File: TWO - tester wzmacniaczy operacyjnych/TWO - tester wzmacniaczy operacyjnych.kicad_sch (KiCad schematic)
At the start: 21 parts

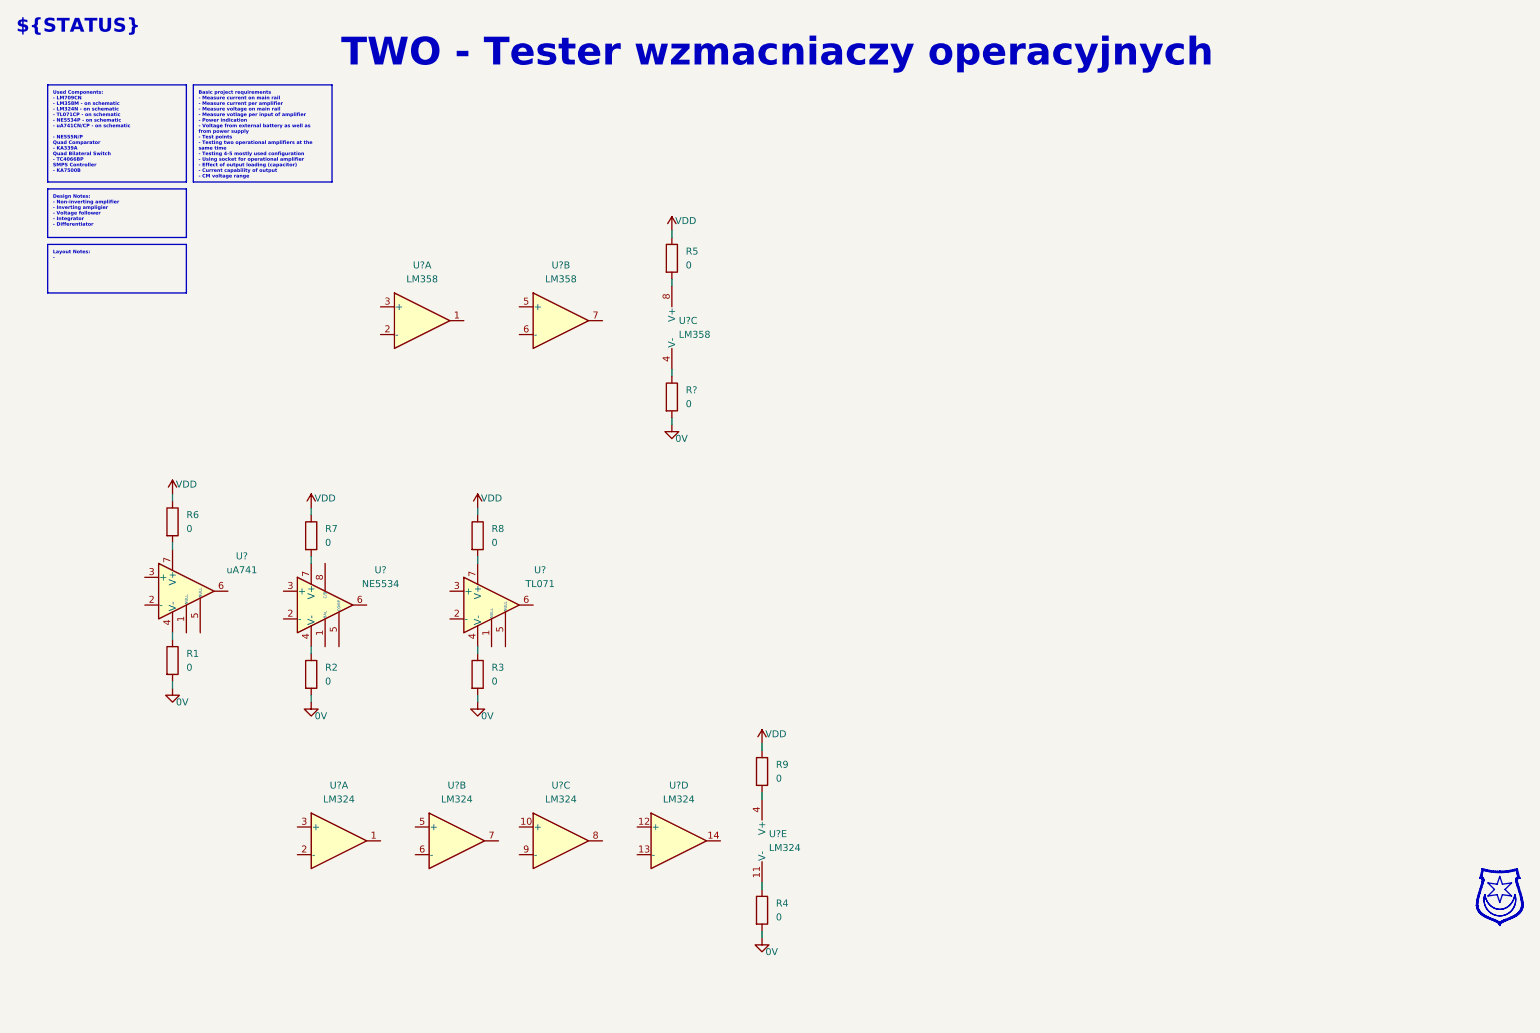
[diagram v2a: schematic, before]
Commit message: Added 50R input, variant with SMD components, input capacitor for AC signal, output capacitance, outputresistor agains short circuit, decoupling capacitors
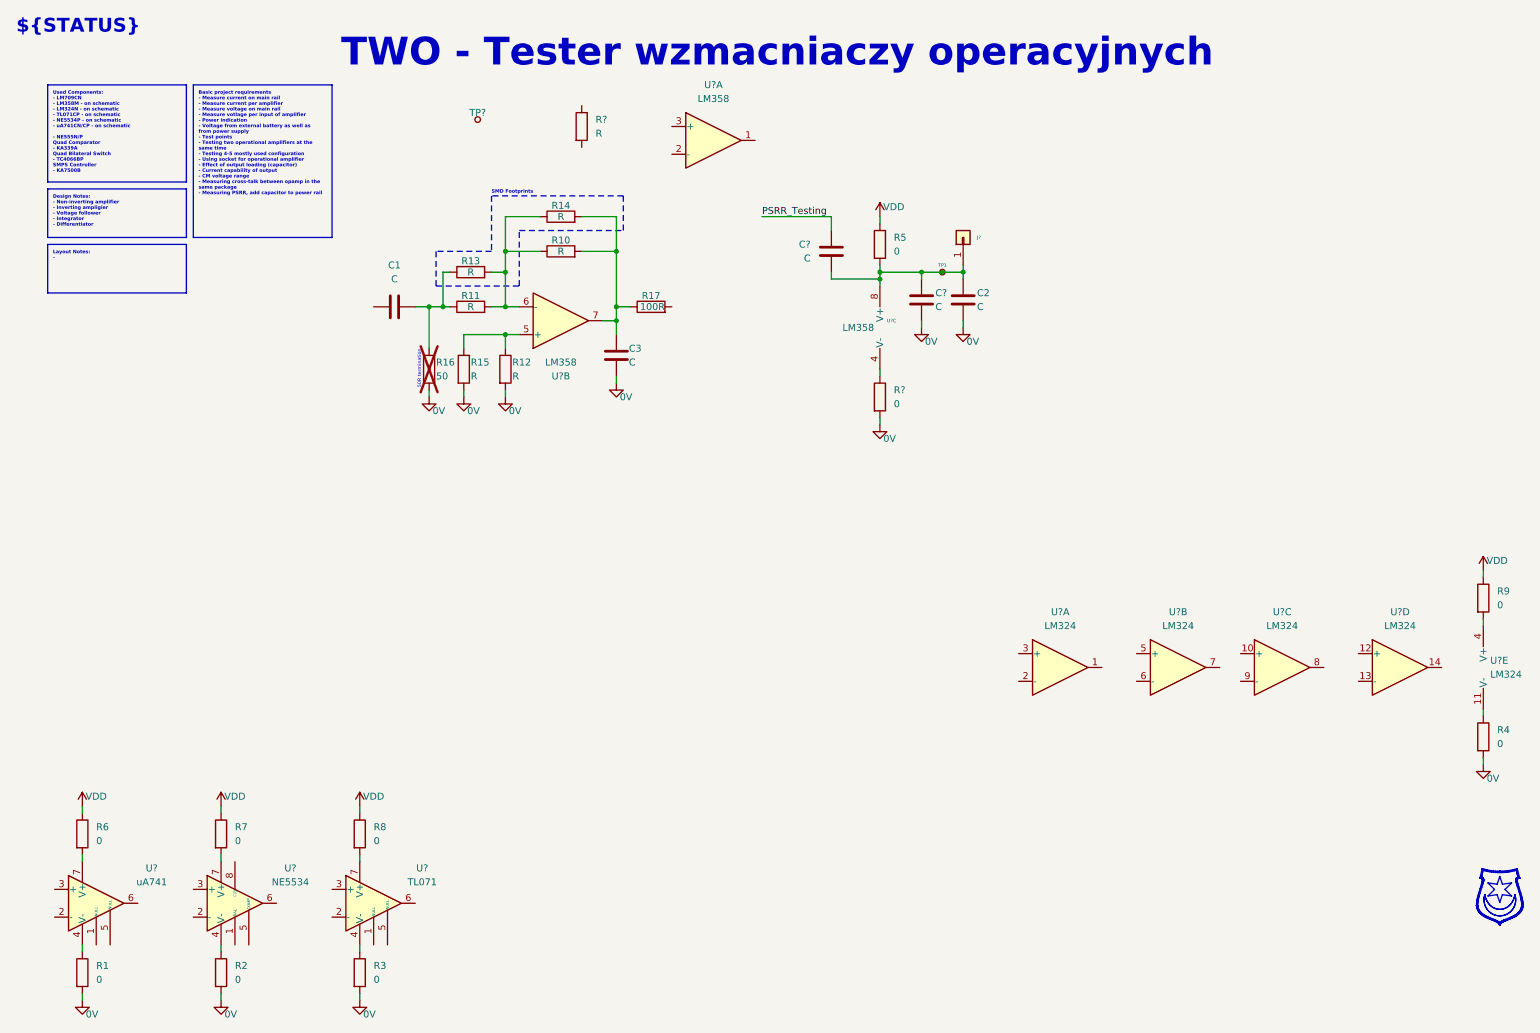
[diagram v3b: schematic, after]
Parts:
- added C1, C3, C?: C, symbol Device:C
- added C2, C?: C, Capacitor_THT:C_Disc_D7.5mm_W2.5mm_P5.00mm, symbol Device:C
- added J?: Conn_01x01, Connector_PinHeader_2.54mm:PinHeader_1x01_P2.54mm_Vertical, symbol Connector_Generic:Conn_01x01
- added R10, R11, R12: R, Resistor_THT:R_Axial_DIN0207_L6.3mm_D2.5mm_P10.16mm_Horizontal, symbol Device:R
- added R13, R14, R15: R, Resistor_SMD:R_0805_2012Metric, symbol Device:R
- added R16: 50, symbol Device:R
- added R17: 100R, symbol Device:R
- added R?: R, symbol Device:R
- added TP1, TP?: TestPoint_Small, symbol Connector:TestPoint_Small
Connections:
- net 0V: now also C2.2, C3.1, C?.2, R12.2, R15.2, R16.2
- net at R5.2, U?.8 (V+): now also C2.1, C?.1, C?.2, J?.1 (Pin_1), TP1.1
- net at U?.5 (+): now also R12.1, R15.1
- net at U?.6 (-): now also R10.1, R11.2, R13.2, R14.1
- net at U?.7: now also C3.2, R10.2, R14.2, R17.1
- new net: C1.2, R11.1, R13.1, R16.1
- new net PSRR_Testing: C?.1
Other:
- note added: "50R termination"
- note added: "SMD Footprints"
- moved on the sheet: R1, R2, R3, R4, R5, R6, R7, R8, R9, R?, U?, U?A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

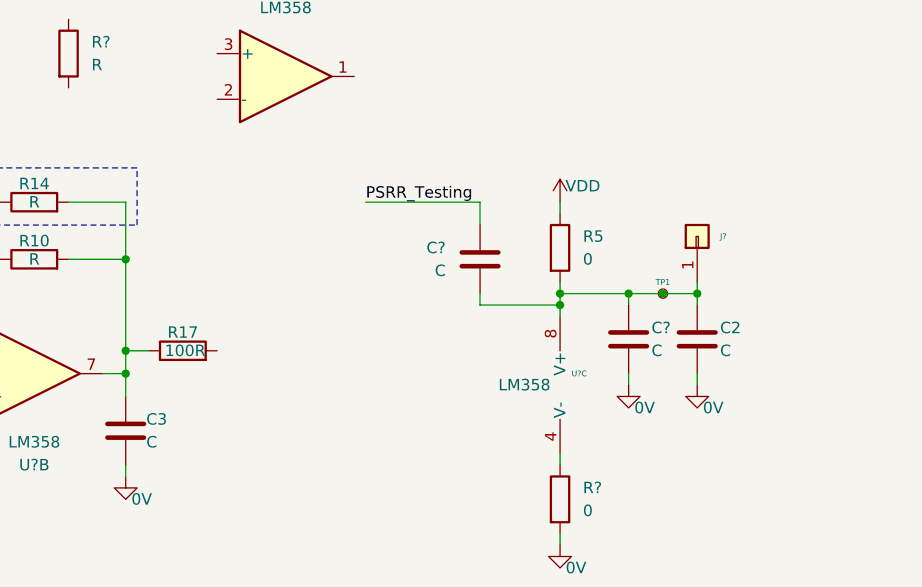
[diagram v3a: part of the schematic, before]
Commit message: Removed schematic in pdf format from project
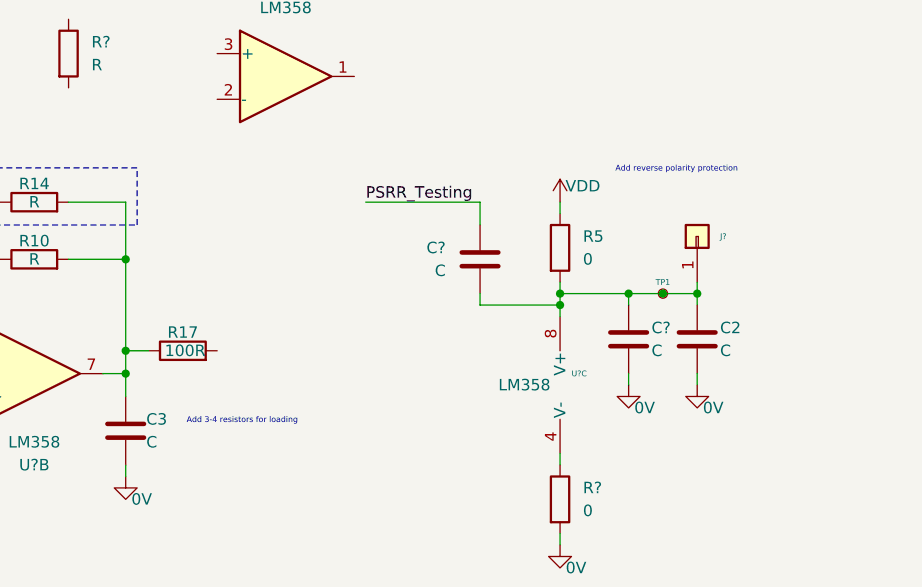
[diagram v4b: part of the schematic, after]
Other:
- note added: "Add 3-4 resistors for loading"
- note added: "Add reverse polarity protection"
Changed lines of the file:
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@@
+		)
+	)
+	(text "Add reverse polarity protection"
+		(exclude_from_sim no)
+		(at 178.054 45.974 0)
+		(effects
+			(font
+				(size 0.635 0.635)
+			)
 		)
 	)
@@
 				(thickness 1.016)
 				(bold yes)
+			)
+		)
+	)
+	(text "Add 3-4 resistors for loading"
+		(exclude_from_sim no)
+		(at 129.794 73.914 0)
+		(effects
+			(font
+				(size 0.635 0.635)
 			)
 		)
@@
 			"AAwAAAACAAAAAQAAAAAAAAAAAAAAAAAAAAAAAAAAAAAAAAAAAAAAAAAAAAAAAAAAAAEAAAAEAAAA"
 			"DAAAABcAAAAiAAAAKAAAACwAAAApAAAAIwAAABoAAAAOAAAABQAAAAEAAAAAAAAAAAAAAAAAAAAA"
-			"AAAAAAAAAAAAAAAAAAAAAAAAAAAAAAAAAAAAAAAAAAAAAAAAAAAAAQAAAA=="
-		)
-	)
+			"AAAAAAAAAAAAAAAAAAAAAAAAAAAAAAAAAAAAAAAAAAAAAAAAAAAAAQAAAAAAAAAAAAAAAAAAAAAA"
+			"AAAAAAAAAAAAAAAAAAAAAAAAAAAAAAAAAAAAAAAAAAAAAAAAAAAAAAAAAAAAAAAAAAAAAAAAAAAA"
+			"AAAAAAAAAAAAAAAAAAAAAAAAAAAAAAAAAAAAAAAAAAAAAAAAAAAAAAAAAAAAAAAAAAAAAAAAAAAA"
+			"AAAAAAAAAAAAAAAAAAAAAAAAAAAAAAAAAAAAAAAAAAAAAAAAAAAAAAAAAAAAAAAAAAAAAAAAAAAA"
+			"AAAAAAAAAAAAAAAAAAAAAAAAAAAAAAAAAAAAAAAAAAAAAAAAAAAAAAAAAAAAAAAAAAAAAAAAAAAA"
+			"AAAAAAAAAAAAAAAAAAAAAAAAAAAAAAAAAAAAAAAAAAAAAAAAAAAAAAAAAAAAAAAAAAAAAAAAAAAA"
+			"AAAAAAAAAAAAAAAAAAAAAAAAAAAAAAAAAAAAAAAAAAAAAAAAAAAAAAAAAAAAAAAAAAAAAAAAAAAA"
+			"AAAAAAAAAAAAAAAAAAAAAAAAAAAAAAAAAAAAAAAAAAAAAAAAAAAAAAAAAAAAAAAAAAAAAAAAAAAA"
+			"AAAAAAAAAAAAAAAAAAAAAAAAAAAAAAAAAAAAAAAAAAAAAAAAAAAAAAAAAAAAAAAAAAAAAAAAAAAA"
+			"AAAAAAAAAAAAAAAAAAAAAAAAAAAAAAAAAAAAAAAAAAAAAAAAAAAAAAAAAAAAAAAAAAAAAAAAAAAA"
+			"AAAAAAAAAAAAAAAAAAAAAAAAAAAAAAAAAAAAAAAAAAAAAAAAAAAAAAAAAAAAAAAAAAAAAAAAAAAA"
+			"AAAAAAAAAAAAAAAAAAAAAAAAAAAAAAAAAAAAAAAAAAAAAAAAAAAAAAAAAAAAAAAAAAAAAAAAAAAA"
+			"AAAAAAAAAAAAAAAAAAAAAAAAAAAAAAAAAAAAAAAAAAAAAAAAAAAAAAAAAAAAAAAAAAAAAAAAAAAA"
+			"AAAAAAAAAAAAAAAAAAAAAAAAAAAAAAAAAAAAAAAAAAAAAAAAAAAAAAAAAAAAAAAAAAAAAAAAAAAA"
+			"AAAAAAAAAAAAAAAAAAAAAAAAAAAAAAAAAAAAAAAAAAAAAAAAAAAAAAAAAAAAAAAAAAAAAAAAAAAA"
+			"AAAAAAAAAAAAAAAAAAAAAAAAAAAAAAAAAAAAAAAAAAAAAAAAAAAAAAAAAAAAAAAAAAAAAAAAAAAA"
+			"AAAAAAAAAAAAAAAAAAAAAAAAAAAAAAAAAAAAAAAAAAAAAAAAAAAAAAAAAAAAAAAAAAAAAAAAAAAA"
+			"AAAAAAAAAAAAAAAAAAAAAAAAAAAAAAAAAAAAAAAAAAAAAAAAAAAAAAAAAAAAAAAAAAAAAAAAAAAA"
+			"AAAAAAAAAAAAAAAAAAAAAAAAAAAAAAAAAAAAAAAAAAAAAAAAAAAAAAAAAA=="
+		)
+	)

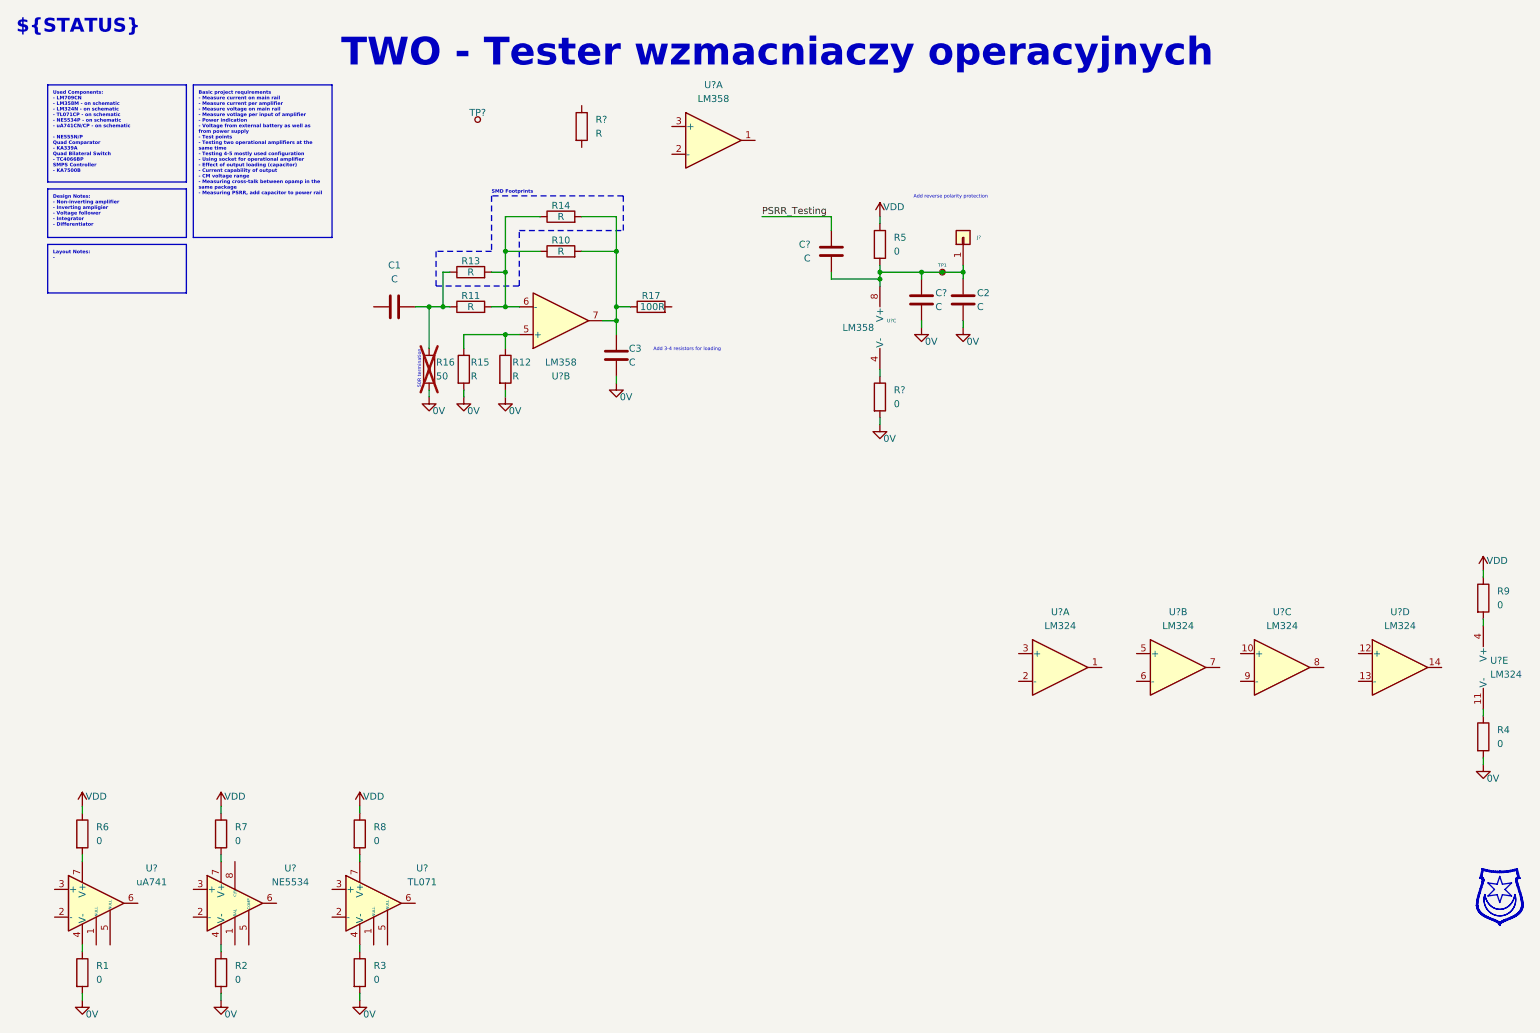
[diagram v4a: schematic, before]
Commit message: Splited schematic into hierarchical design
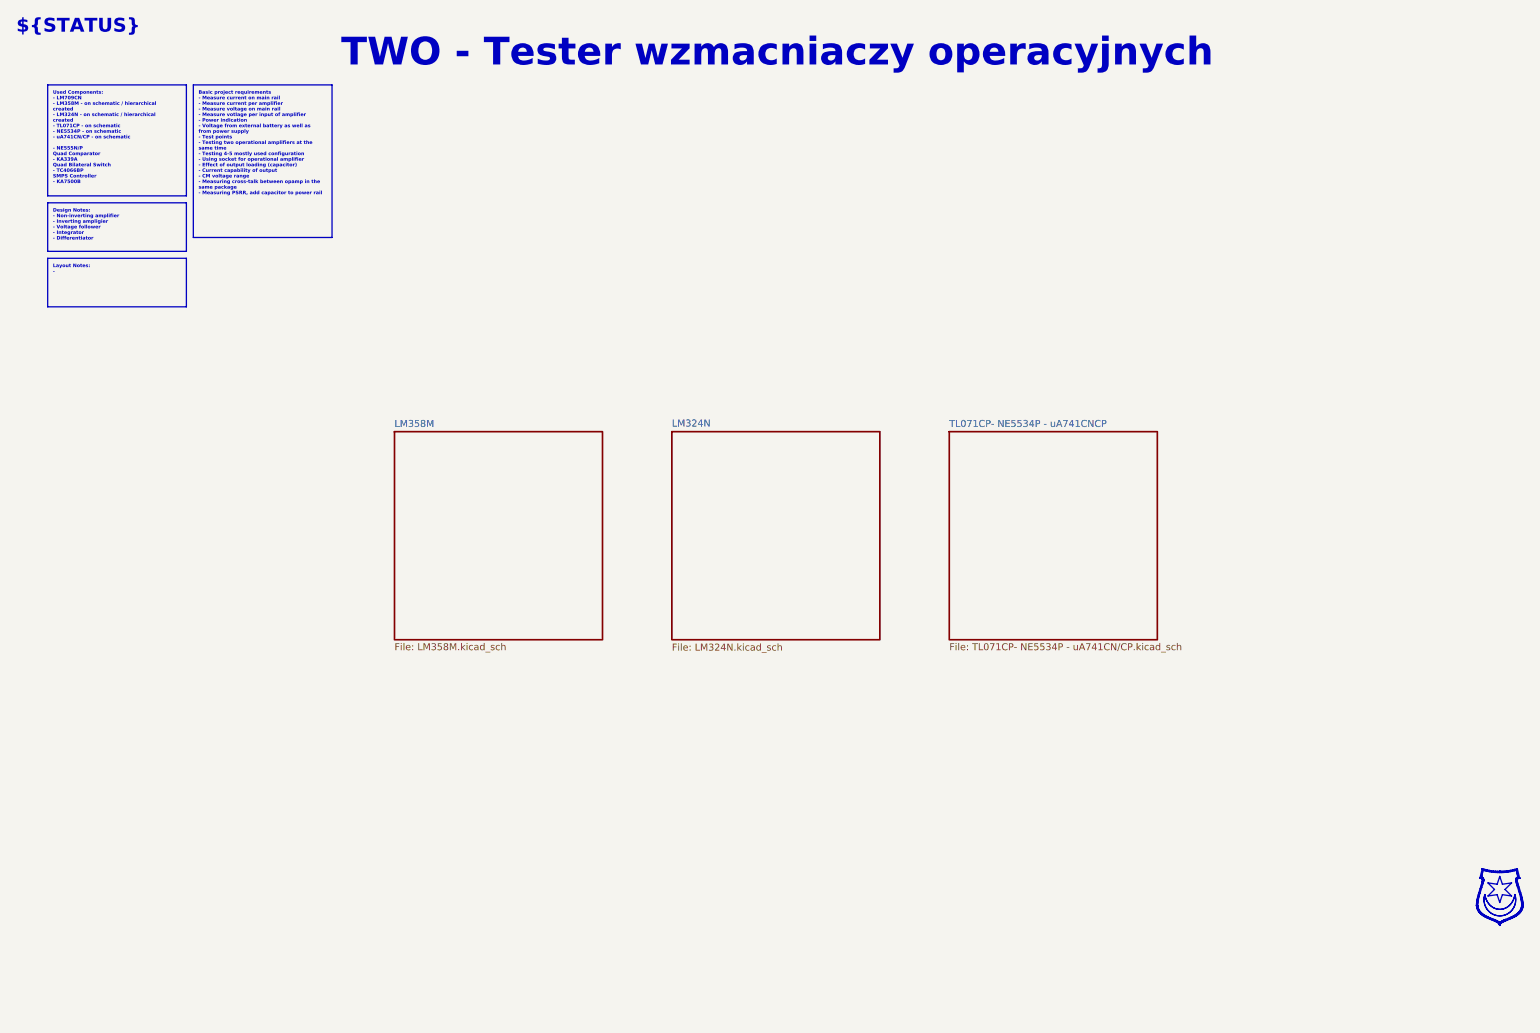
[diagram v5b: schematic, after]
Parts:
- removed C1, C3, C?: C, symbol Device:C
- removed C2, C?: C, Capacitor_THT:C_Disc_D7.5mm_W2.5mm_P5.00mm, symbol Device:C
- removed J?: Conn_01x01, Connector_PinHeader_2.54mm:PinHeader_1x01_P2.54mm_Vertical, symbol Connector_Generic:Conn_01x01
- removed R1, R2, R3, R4, R5, R6, R7, R8, R9, R?: 0, symbol Device:R
- removed R10, R11, R12: R, Resistor_THT:R_Axial_DIN0207_L6.3mm_D2.5mm_P10.16mm_Horizontal, symbol Device:R
- removed R13, R14, R15: R, Resistor_SMD:R_0805_2012Metric, symbol Device:R
- removed R16: 50, symbol Device:R
- removed R17: 100R, symbol Device:R
- removed R?: R, symbol Device:R
- removed TP1, TP?: TestPoint_Small, symbol Connector:TestPoint_Small
- removed U? (x5): LM324, symbol Amplifier_Operational:LM324
- removed U?: NE5534, symbol Amplifier_Operational:NE5534
- removed U?: uA741, symbol Amplifier_Operational:LM741
- removed U? (x3): LM358, Package_DIP:DIP-8_W7.62mm_Socket, symbol Amplifier_Operational:LM358
- removed U?: TL071, symbol Amplifier_Operational:TL071
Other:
- added sheet LM324N (LM324N.kicad_sch)
- added sheet LM358M (LM358M.kicad_sch)
- added sheet TL071CP- NE5534P - uA741CNCP (TL071CP- NE5534P - uA741CN/CP.kicad_sch)
- note removed: "50R termination"
- note removed: "Add 3-4 resistors for loading"
- note removed: "Add reverse polarity protection"
- note removed: "SMD Footprints"
